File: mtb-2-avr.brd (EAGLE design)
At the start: 27 x 22 mm, 15 parts, among them IC1 MEGA328P-AU, Q1 14.745 MHz

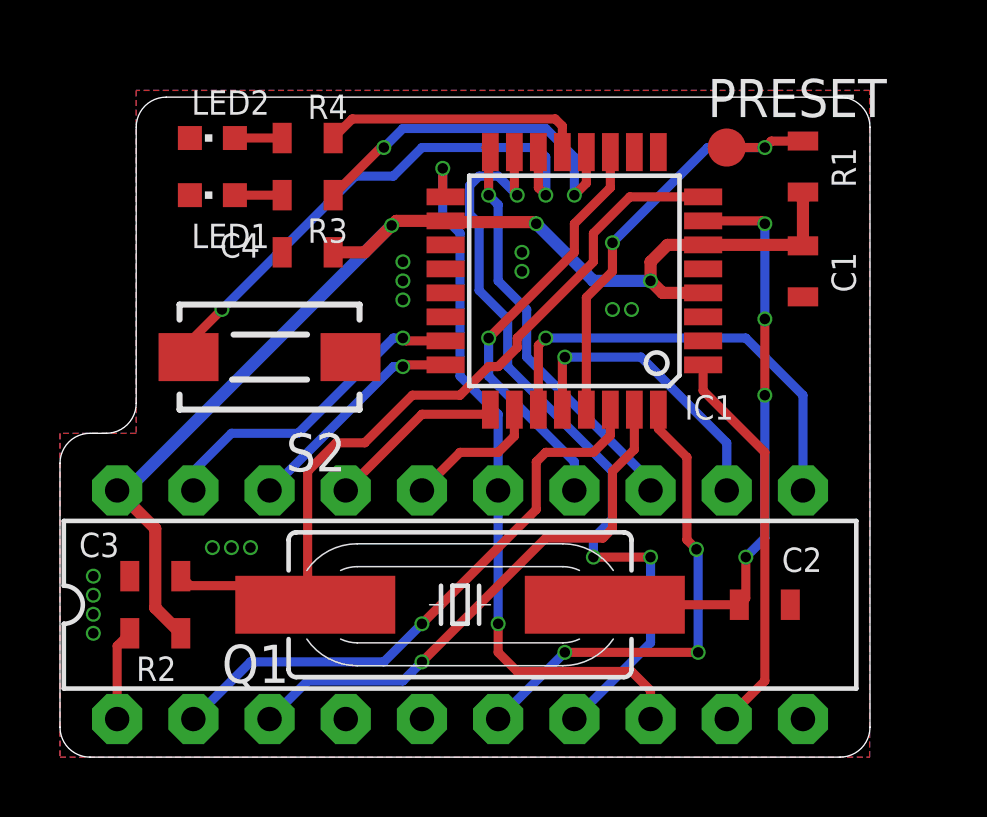
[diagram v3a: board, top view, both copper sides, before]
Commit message: Use ATmega8A, fix silksreen.
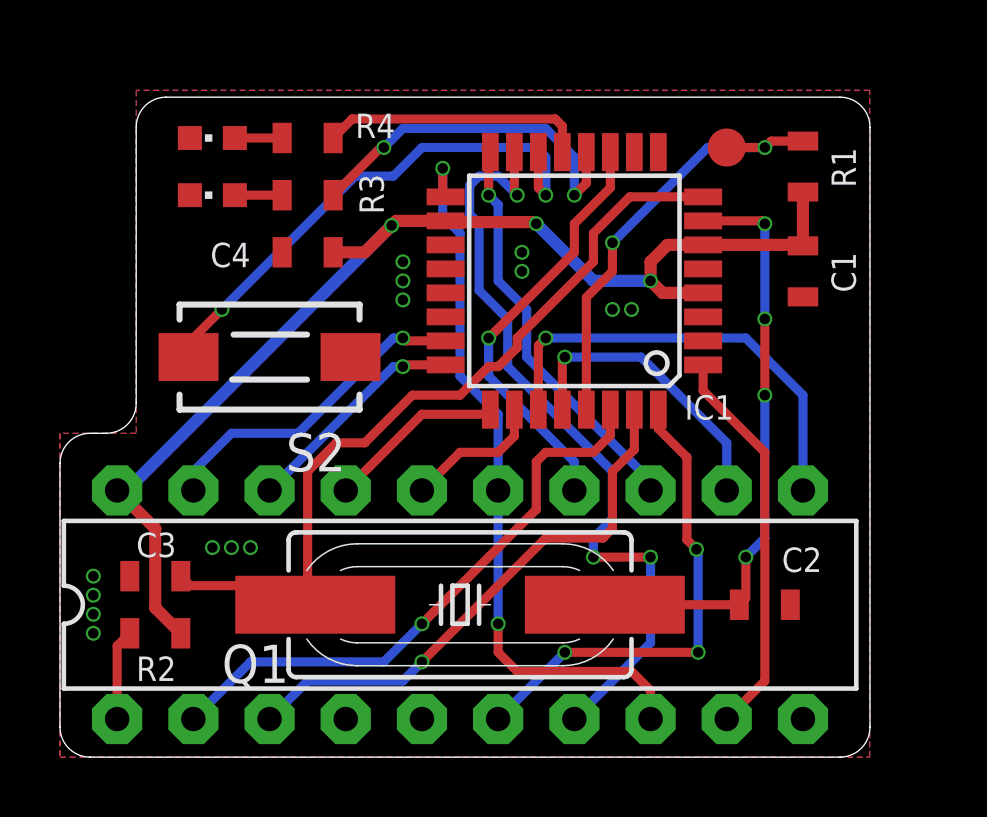
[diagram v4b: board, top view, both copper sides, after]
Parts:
- IC1: value MEGA328P-AU -> MEGA8AA-AU
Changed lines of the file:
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@@
 </autorouter>
 <elements>
-<element name="IC1" library="atmel" library_urn="urn:adsk.eagle:library:105" package="TQFP32-08" package3d_urn="urn:adsk.eagle:package:4313/2" value="MEGA328P-AU" x="17.145" y="15.875" smashed="yes" rot="R180">
-<attribute name="LCSC_PART" value="C14877" x="17.145" y="15.875" size="1.778" layer="27" rot="R180" display="off"/>
+<element name="IC1" library="atmel" library_urn="urn:adsk.eagle:library:105" package="TQFP32-08" package3d_urn="urn:adsk.eagle:package:4313/2" value="MEGA8AA-AU" x="17.145" y="15.875" smashed="yes" rot="R180">
+<attribute name="LCSC_PART" value="C16190" x="17.145" y="15.875" size="1.778" layer="27" rot="R180" display="off"/>
 <attribute name="MF" value="" x="-0.635" y="20.955" size="1.778" layer="27" rot="R180" display="off"/>
 <attribute name="MPN" value="ATMEGA8-16AU" x="-0.635" y="20.955" size="1.778" layer="27" rot="R180" display="off"/>
@@
 <attribute name="OC_NEWARK" value="73M8863" x="-0.635" y="20.955" size="1.778" layer="27" rot="R180" display="off"/>
 <attribute name="POPULARITY" value="11" x="-0.635" y="20.955" size="1.778" layer="27" rot="R180" display="off"/>
-<attribute name="VALUE" x="20.1676" y="17.145" size="0.8128" layer="27" rot="R180"/>
+<attribute name="VALUE" x="22.225" y="19.5326" size="0.8128" layer="27" rot="R270"/>
 </element>
 <element name="TORIG" library="mtb-2" package="DIL20" value="" x="13.335" y="5.08" smashed="yes"/>
@@
 <attribute name="LCSC_PART" value="C14663" x="24.765" y="16.1925" size="1.778" layer="27" rot="R270" display="off"/>
 <attribute name="NAME" x="25.7175" y="16.8275" size="0.8128" layer="25" rot="R270"/>
-<attribute name="VALUE" x="22.225" y="17.4625" size="1.27" layer="27" rot="R270"/>
+<attribute name="VALUE" x="25.7175" y="17.145" size="0.8128" layer="27" rot="R270"/>
 </element>
 <element name="R1" library="rcl" package="R0603" value="10k" x="24.765" y="19.685" smashed="yes" rot="R270">
 <attribute name="LCSC_PART" value="C25804" x="24.765" y="19.685" size="1.778" layer="27" rot="R270" display="off"/>
 <attribute name="NAME" x="25.7175" y="20.32" size="0.8128" layer="25" rot="R270"/>
-<attribute name="VALUE" x="22.225" y="20.955" size="1.27" layer="27" rot="R270"/>
+<attribute name="VALUE" x="25.7175" y="20.6375" size="0.8128" layer="27" rot="R270"/>
 </element>
 <element name="LED1" library="led" library_urn="urn:adsk.eagle:library:259" package="CHIPLED_0603" package3d_urn="urn:adsk.eagle:package:15822/2" value="GREEN" x="5.08" y="18.7325" smashed="yes" rot="R90">
 <attribute name="LCSC_PART" value="C72043" x="5.08" y="18.7325" size="1.778" layer="27" rot="R90" display="off"/>
-<attribute name="NAME" x="6.985" y="17.78" size="0.8128" layer="25" rot="R180"/>
 <attribute name="POPULARITY" value="28" x="5.08" y="18.7325" size="1.778" layer="27" rot="R90" display="off"/>
-<attribute name="VALUE" x="6.35" y="21.2725" size="1.27" layer="27" rot="R180"/>
 </element>
 <element name="LED2" library="led" library_urn="urn:adsk.eagle:library:259" package="CHIPLED_0603" package3d_urn="urn:adsk.eagle:package:15822/2" value="BLUE" x="5.08" y="20.6375" smashed="yes" rot="R90">
 <attribute name="LCSC_PART" value="C72041" x="5.08" y="20.6375" size="1.778" layer="27" rot="R90" display="off"/>
-<attribute name="NAME" x="6.985" y="22.225" size="0.8128" layer="25" rot="R180"/>
 <attribute name="POPULARITY" value="28" x="5.08" y="20.6375" size="1.778" layer="27" rot="R90" display="off"/>
-<attribute name="VALUE" x="6.35" y="23.1775" size="1.27" layer="27" rot="R180"/>
 </element>
 <element name="Q1" library="crystal" library_urn="urn:adsk.eagle:library:204" package="HC49UP" package3d_urn="urn:adsk.eagle:package:12078/1" value="14.745 MHz" x="13.335" y="5.08" smashed="yes">
@@
 <attribute name="OC_NEWARK" value="unknown" x="13.335" y="5.08" size="1.778" layer="27" display="off"/>
 <attribute name="POPULARITY" value="19" x="13.335" y="5.08" size="1.778" layer="27" display="off"/>
-<attribute name="VALUE" x="7.62" y="0.889" size="1.27" layer="27" ratio="10"/>
+<attribute name="VALUE" x="9.8425" y="5.969" size="0.8128" layer="27" ratio="10"/>
 </element>
 <element name="C2" library="rcl" package="C0603" value="22p" x="23.495" y="5.08" smashed="yes" rot="R180">
 <attribute name="LCSC_PART" value="C1653" x="23.495" y="5.08" size="1.778" layer="27" rot="R180" display="off"/>
 <attribute name="NAME" x="25.4" y="6.985" size="0.8128" layer="25" rot="R180"/>
-<attribute name="VALUE" x="24.765" y="7.62" size="1.27" layer="27" rot="R180"/>
+<attribute name="VALUE" x="24.765" y="4.1275" size="0.8128" layer="27" rot="R180"/>
 </element>
 <element name="C3" library="rcl" package="C0603" value="22p" x="3.175" y="6.0325" smashed="yes">
 <attribute name="LCSC_PART" value="C1653" x="3.175" y="6.0325" size="1.778" layer="27" display="off"/>
-<attribute name="NAME" x="0.635" y="6.6675" size="0.8128" layer="25"/>
-<attribute name="VALUE" x="1.905" y="3.4925" size="1.27" layer="27"/>
+<attribute name="NAME" x="2.54" y="6.6675" size="0.8128" layer="25"/>
+<attribute name="VALUE" x="4.445" y="5.715" size="0.8128" layer="27"/>
 </element>
 <element name="C4" library="rcl" package="C0603" value="100n" x="8.255" y="16.8275" smashed="yes" rot="R180">
 <attribute name="LCSC_PART" value="C14663" x="8.255" y="16.8275" size="1.778" layer="27" rot="R180" display="off"/>
-<attribute name="NAME" x="6.6675" y="17.4625" size="0.8128" layer="25" rot="R180"/>
-<attribute name="VALUE" x="9.525" y="19.3675" size="1.27" layer="27" rot="R180"/>
+<attribute name="NAME" x="6.35" y="17.145" size="0.8128" layer="25" rot="R180"/>
+<attribute name="VALUE" x="6.985" y="17.145" size="0.8128" layer="27" rot="R180"/>
 </element>
 <element name="R2" library="rcl" package="R0603" value="10k" x="3.175" y="4.1275" smashed="yes">
 <attribute name="LCSC_PART" value="C25804" x="3.175" y="4.1275" size="1.778" layer="27" display="off"/>
 <attribute name="NAME" x="2.54" y="2.54" size="0.8128" layer="25"/>
-<attribute name="VALUE" x="2.54" y="1.5875" size="1.27" layer="27"/>
+<attribute name="VALUE" x="4.445" y="3.81" size="0.8128" layer="27"/>
 </element>
 <element name="R3" library="rcl" package="R0603" value="10k" x="8.255" y="18.7325" smashed="yes">
 <attribute name="LCSC_PART" value="C25804" x="8.255" y="18.7325" size="1.778" layer="27" display="off"/>
-<attribute name="NAME" x="8.255" y="17.145" size="0.8128" layer="25"/>
-<attribute name="VALUE" x="7.62" y="16.1925" size="1.27" layer="27"/>
+<attribute name="NAME" x="10.795" y="18.0975" size="0.8128" layer="25" rot="R90"/>
+<attribute name="VALUE" x="9.525" y="18.7325" size="0.8128" layer="27"/>
 </element>
 <element name="R4" library="rcl" package="R0603" value="1k" x="8.255" y="20.6375" smashed="yes">
 <attribute name="LCSC_PART" value="C21190" x="8.255" y="20.6375" size="1.778" layer="27" display="off"/>
-<attribute name="NAME" x="8.255" y="21.2725" size="0.8128" layer="25"/>
-<attribute name="VALUE" x="7.62" y="18.0975" size="1.27" layer="27"/>
+<attribute name="NAME" x="9.8425" y="20.6375" size="0.8128" layer="25"/>
+<attribute name="VALUE" x="9.8425" y="20.6375" size="0.8128" layer="27"/>
 </element>
 <element name="PRESET" library="testpad" library_urn="urn:adsk.eagle:library:385" package="B1,27" package3d_urn="urn:adsk.eagle:package:27944/2" value="PTR1B1,27" x="22.225" y="20.32" smashed="yes">
-<attribute name="NAME" x="21.59" y="21.336" size="1.27" layer="25" ratio="10"/>
 <attribute name="POPULARITY" value="2" x="22.225" y="20.32" size="1.778" layer="27" display="off"/>
 <attribute name="TP_SIGNAL_NAME" value="" x="22.225" y="20.32" size="1.778" layer="27" display="off"/>
@@
 </element>
 <element name="S2" library="switch-tact" package="DTSM-3" value="DTSM-3" x="6.985" y="13.335" smashed="yes" rot="R180">
+<attribute name="LCSC_PART" value="C318938" x="6.985" y="13.335" size="1.778" layer="27" rot="R180" display="off"/>
 <attribute name="NAME" x="9.525" y="10.795" size="1.27" layer="25" rot="R180"/>
-<attribute name="VALUE" x="9.525" y="17.145" size="1.27" layer="27" rot="R180"/>
+<attribute name="VALUE" x="9.2075" y="11.1125" size="0.8128" layer="27" rot="R180"/>
 </element>
 </elements>

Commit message: Silkscreen tweaks.
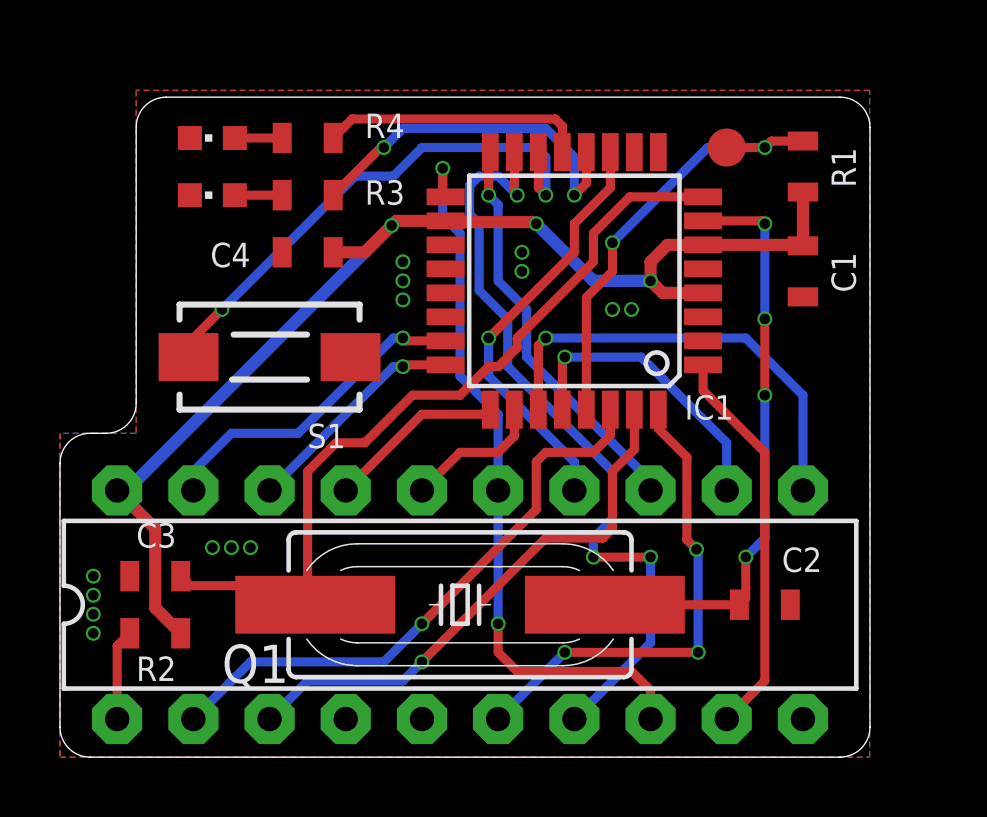
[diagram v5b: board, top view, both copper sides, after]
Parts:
- IC1: value MEGA8AA-AU -> MEGA8A-AU
- renumbered S2 to S1
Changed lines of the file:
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@@
 <layer number="25" name="tNames" color="7" fill="1" visible="no" active="yes"/>
 <layer number="26" name="bNames" color="7" fill="1" visible="no" active="yes"/>
-<layer number="27" name="tValues" color="7" fill="1" visible="no" active="yes"/>
+<layer number="27" name="tValues" color="7" fill="1" visible="yes" active="yes"/>
 <layer number="28" name="bValues" color="7" fill="1" visible="no" active="yes"/>
 <layer number="29" name="tStop" color="7" fill="3" visible="no" active="yes"/>
@@
 </autorouter>
 <elements>
-<element name="IC1" library="atmel" library_urn="urn:adsk.eagle:library:105" package="TQFP32-08" package3d_urn="urn:adsk.eagle:package:4313/2" value="MEGA8AA-AU" x="17.145" y="15.875" smashed="yes" rot="R180">
+<element name="IC1" library="atmel" library_urn="urn:adsk.eagle:library:105" package="TQFP32-08" package3d_urn="urn:adsk.eagle:package:4313/2" value="MEGA8A-AU" x="17.145" y="15.875" smashed="yes" rot="R180">
 <attribute name="LCSC_PART" value="C16190" x="17.145" y="15.875" size="1.778" layer="27" rot="R180" display="off"/>
 <attribute name="MF" value="" x="-0.635" y="20.955" size="1.778" layer="27" rot="R180" display="off"/>
@@
 <element name="C3" library="rcl" package="C0603" value="22p" x="3.175" y="6.0325" smashed="yes">
 <attribute name="LCSC_PART" value="C1653" x="3.175" y="6.0325" size="1.778" layer="27" display="off"/>
-<attribute name="NAME" x="2.54" y="6.6675" size="0.8128" layer="25"/>
+<attribute name="NAME" x="2.54" y="6.985" size="0.8128" layer="25"/>
 <attribute name="VALUE" x="4.445" y="5.715" size="0.8128" layer="27"/>
 </element>
@@
 <element name="R3" library="rcl" package="R0603" value="10k" x="8.255" y="18.7325" smashed="yes">
 <attribute name="LCSC_PART" value="C25804" x="8.255" y="18.7325" size="1.778" layer="27" display="off"/>
-<attribute name="NAME" x="10.795" y="18.0975" size="0.8128" layer="25" rot="R90"/>
+<attribute name="NAME" x="10.16" y="18.415" size="0.8128" layer="25"/>
 <attribute name="VALUE" x="9.525" y="18.7325" size="0.8128" layer="27"/>
 </element>
 <element name="R4" library="rcl" package="R0603" value="1k" x="8.255" y="20.6375" smashed="yes">
 <attribute name="LCSC_PART" value="C21190" x="8.255" y="20.6375" size="1.778" layer="27" display="off"/>
-<attribute name="NAME" x="9.8425" y="20.6375" size="0.8128" layer="25"/>
+<attribute name="NAME" x="10.16" y="20.6375" size="0.8128" layer="25"/>
 <attribute name="VALUE" x="9.8425" y="20.6375" size="0.8128" layer="27"/>
 </element>
@@
 <attribute name="VALUE" x="21.59" y="19.558" size="0.0254" layer="27"/>
 </element>
-<element name="S2" library="switch-tact" package="DTSM-3" value="DTSM-3" x="6.985" y="13.335" smashed="yes" rot="R180">
-<attribute name="LCSC_PART" value="C318938" x="6.985" y="13.335" size="1.778" layer="27" rot="R180" display="off"/>
-<attribute name="NAME" x="9.525" y="10.795" size="1.27" layer="25" rot="R180"/>
+<element name="S1" library="switch-tact" package="DTSM-3" value="DTSM-3" x="6.985" y="13.335" smashed="yes" rot="R180">
+<attribute name="LCSC_PART" value="C557591" x="6.985" y="13.335" size="1.778" layer="27" rot="R180" display="off"/>
+<attribute name="NAME" x="9.525" y="11.1125" size="0.8128" layer="25" rot="R180"/>
 <attribute name="VALUE" x="9.2075" y="11.1125" size="0.8128" layer="27" rot="R180"/>
 </element>
@@
 <via x="11.43" y="15.24" extent="1-16" drill="0.35"/>
 <via x="15.39875" y="16.8275" extent="1-16" drill="0.35"/>
-<contactref element="S2" pad="1"/>
+<contactref element="S1" pad="1"/>
 </signal>
 <signal name="VCC">
@@
 </signal>
 <signal name="N$5">
-<contactref element="S2" pad="2"/>
+<contactref element="S1" pad="2"/>
 <contactref element="IC1" pad="14"/>
 <wire x1="15.945" y1="20.1676" x2="15.945" y2="18.98" width="0.3048" layer="1"/>
